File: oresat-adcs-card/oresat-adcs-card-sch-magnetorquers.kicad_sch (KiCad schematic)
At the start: 80 parts, among them U16 STSPIN250, U21 INA185, U22 STSPIN250, U23 INA185, U3 STSPIN250, U4 INA185

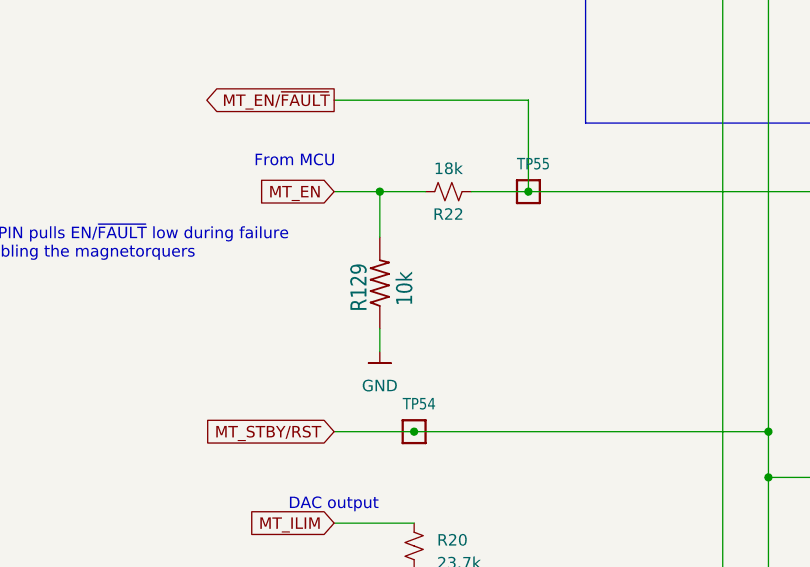
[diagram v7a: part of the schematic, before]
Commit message: Upgrade to KiCAD 8!
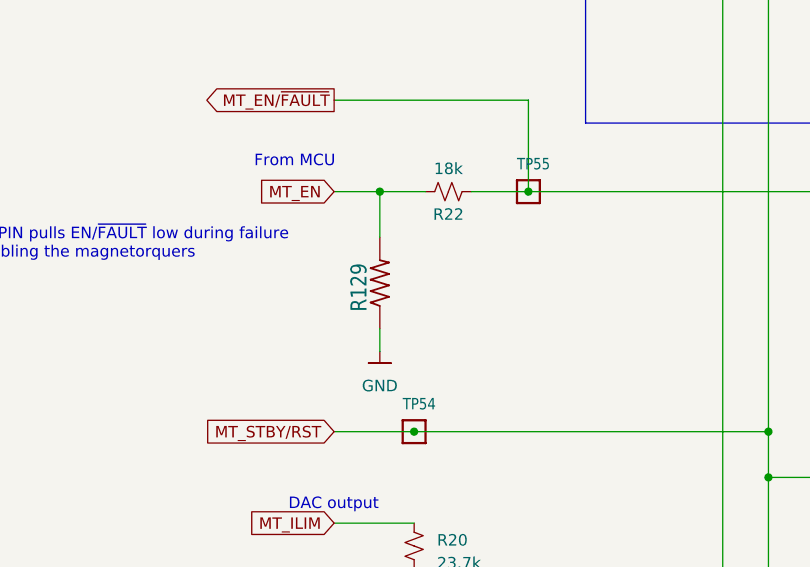
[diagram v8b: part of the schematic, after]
